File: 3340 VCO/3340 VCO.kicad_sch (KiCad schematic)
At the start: 99 parts, among them J1 AudioJack2_SwitchT, J2 AudioJack2_SwitchT, J3 AudioJack2_SwitchT, J4 AudioJack2_SwitchT, J5 AudioJack2_SwitchT, J6 Conn_02x05_Odd_Even, J7 AudioJack2_SwitchT, J8 AudioJack2_SwitchT, J9 AudioJack2_SwitchT, SW1 SW_SPDT, U1 TL072, U2 TL072, U3 TL072, U4 AS3340

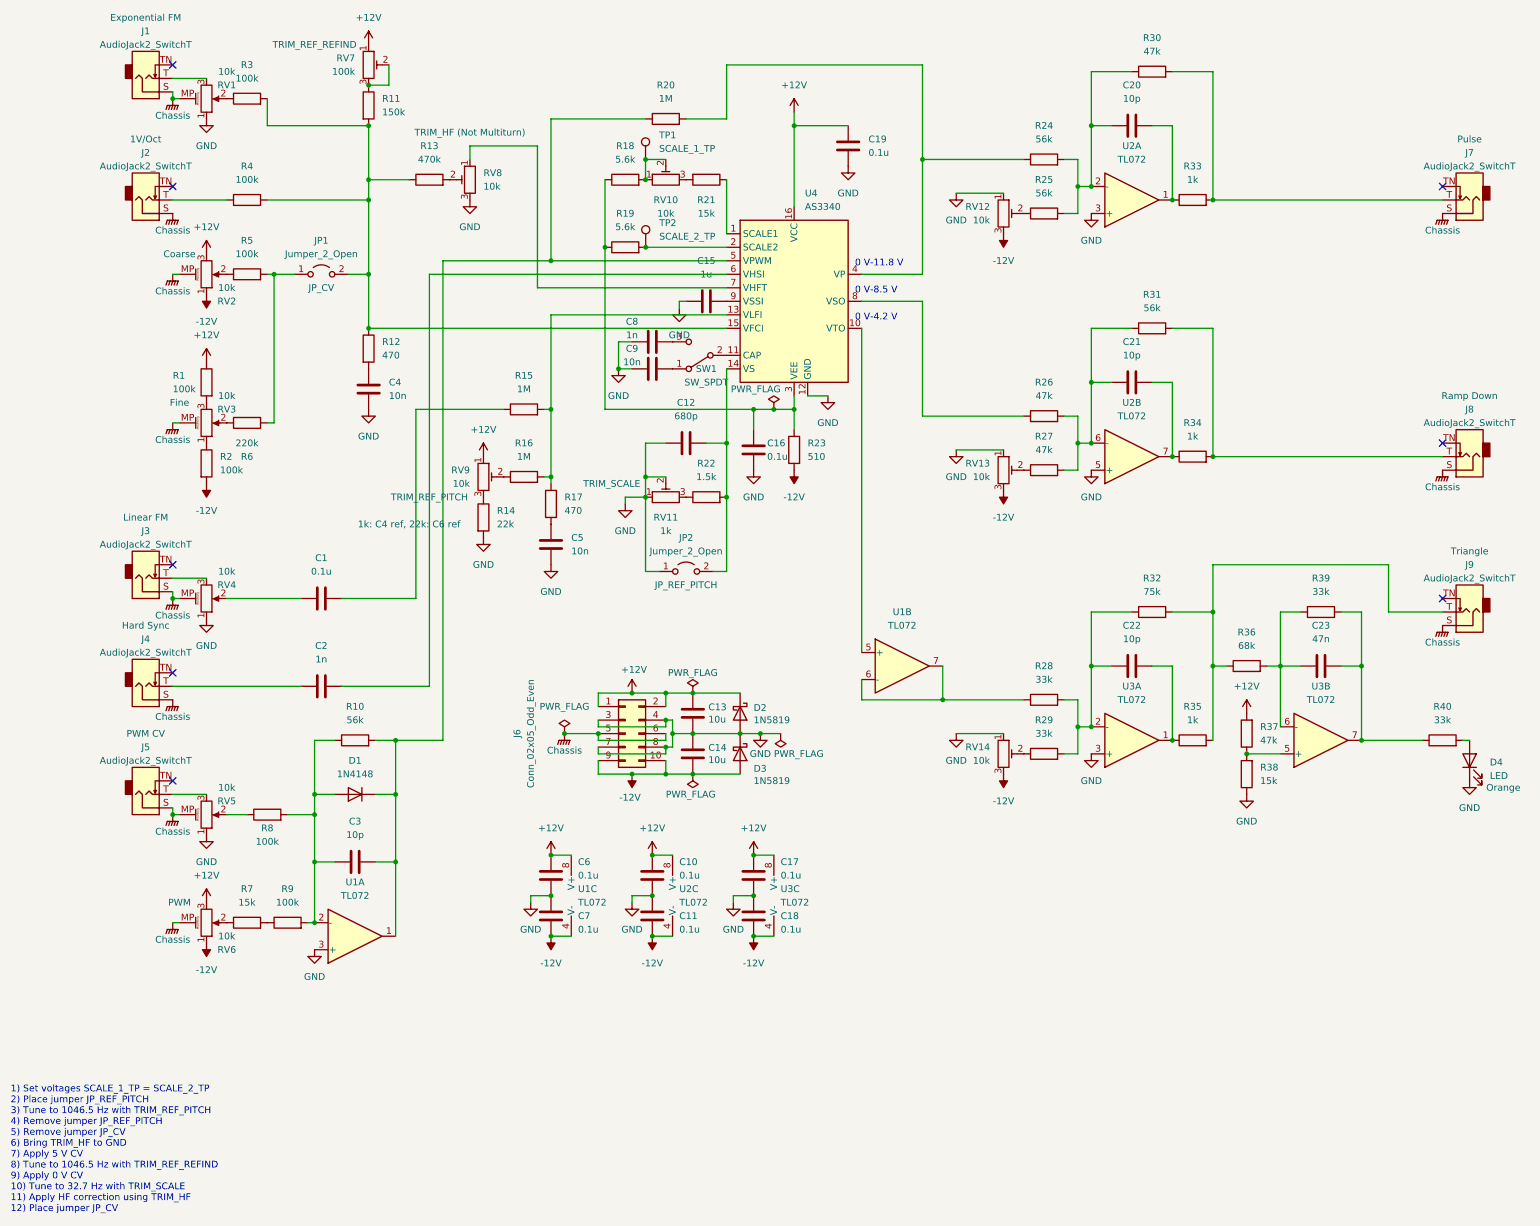
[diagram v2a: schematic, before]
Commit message: Create separate front end VCO board
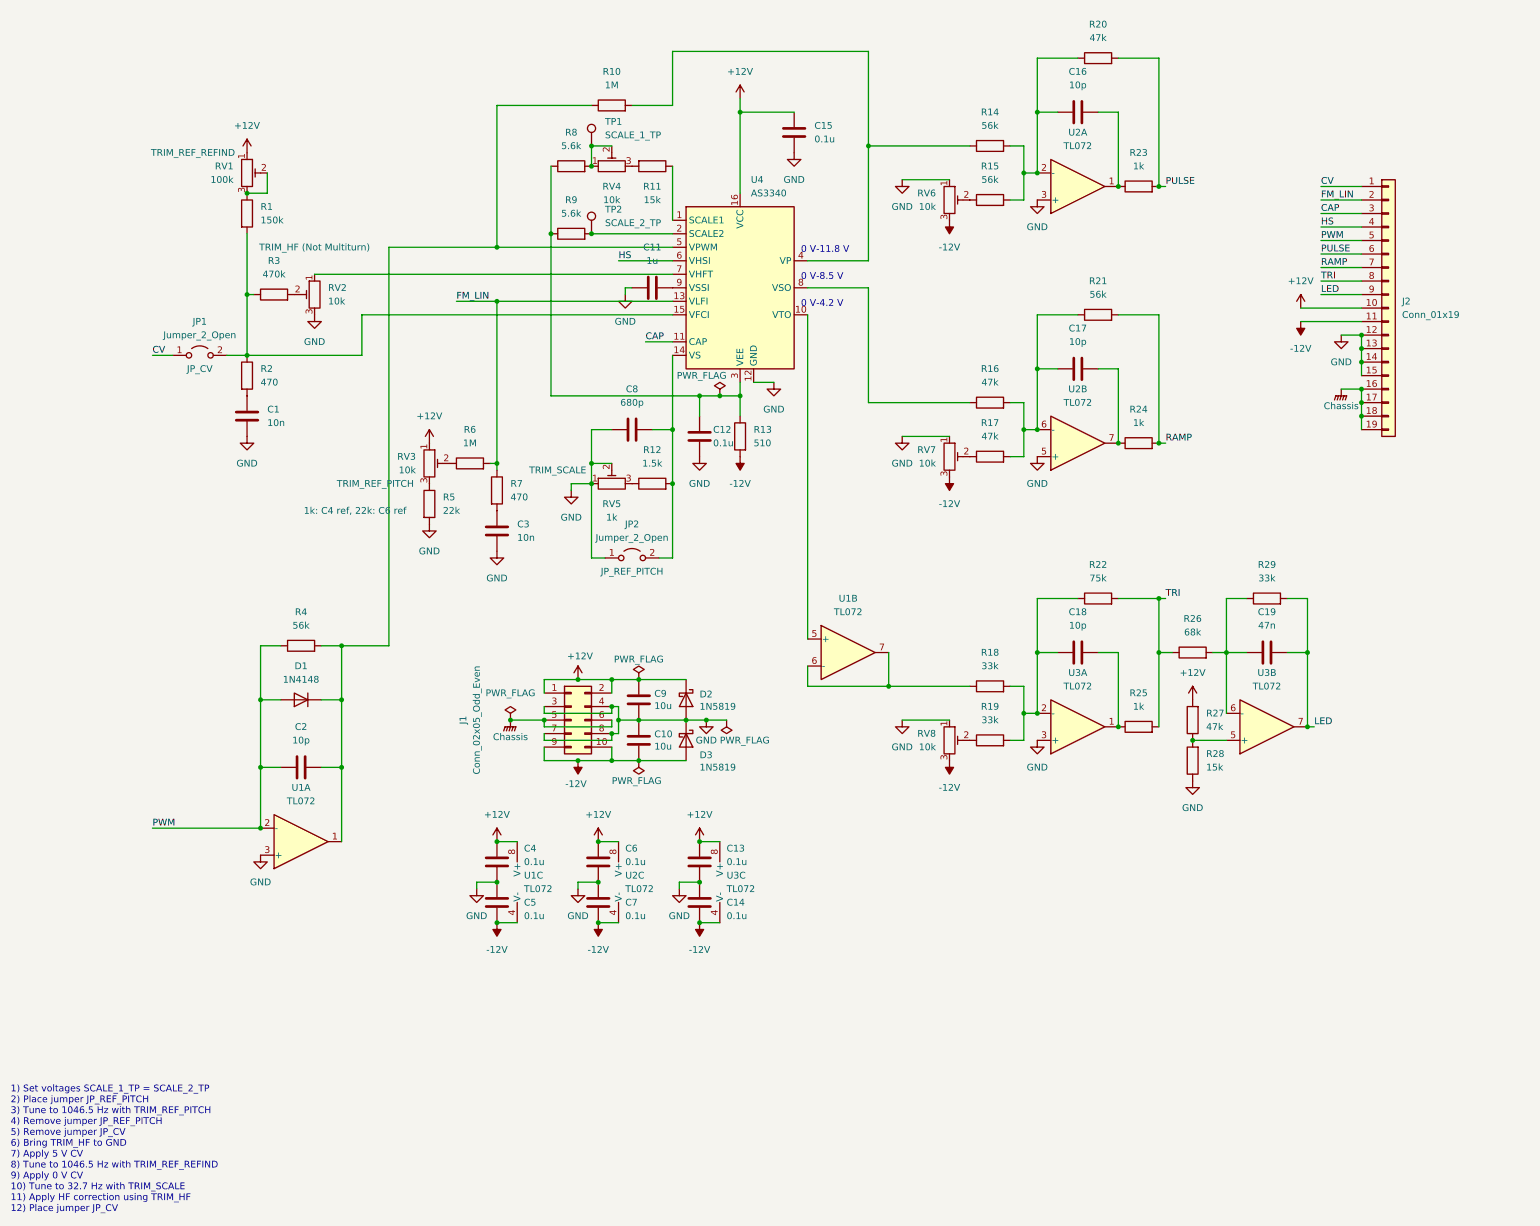
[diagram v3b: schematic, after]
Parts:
- removed C1: 0.1u, 0_Capacitor_THT:C_Disc_D5.5mm_W2.5mm_P2.50mm, symbol Device:C
- removed C2, C8: 1n, 0_Capacitor_THT:C_Disc_D5.5mm_W2.5mm_P2.50mm, symbol Device:C
- removed C9: 10n, 0_Capacitor_THT:C_Disc_D5.5mm_W2.5mm_P2.50mm, symbol Device:C
- removed D4: LED, LED_THT:LED_D5.0mm, symbol Device:LED
- removed J1, J2, J3, J4, J5, J7, J8, J9: AudioJack2_SwitchT, Connector_Audio:Jack_3.5mm_QingPu_WQP-PJ398SM_Vertical_CircularHoles, symbol Connector:AudioJack2_SwitchT
- removed R1, R2, R4, R5, R8, R9: 100k, Resistor_THT:R_Axial_DIN0207_L6.3mm_D2.5mm_P7.62mm_Horizontal, symbol Device:R
- removed R13: 470k, Resistor_THT:R_Axial_DIN0207_L6.3mm_D2.5mm_P7.62mm_Horizontal, symbol Device:R
- removed R15: 1M, Resistor_THT:R_Axial_DIN0207_L6.3mm_D2.5mm_P7.62mm_Horizontal, symbol Device:R
- removed R40: 33k, Resistor_THT:R_Axial_DIN0207_L6.3mm_D2.5mm_P7.62mm_Horizontal, symbol Device:R
- removed R6: 220k, Resistor_THT:R_Axial_DIN0207_L6.3mm_D2.5mm_P7.62mm_Horizontal, symbol Device:R
- removed R7: 15k, Resistor_THT:R_Axial_DIN0207_L6.3mm_D2.5mm_P7.62mm_Horizontal, symbol Device:R
- removed RV1, RV2, RV3, RV4, RV5, RV6: 10k, 0_Potentiometer_THT:Potentiometer_Alpha_RD901F-40-00D_Single_Vertical_MP, symbol Device:R_Potentiometer_MountingPin
- removed RV8: 10k, Potentiometer_THT:Potentiometer_Runtron_RM-065_Vertical, symbol Device:R_Potentiometer_Trim
- removed SW1: SW_SPDT, 0_Switch_THT:MTS-102_MTS-103_MTS-112_MTS-113_MTS-123, symbol Switch:SW_SPDT
- added J2: Conn_01x19, Connector_PinHeader_2.54mm:PinHeader_1x19_P2.54mm_Vertical, symbol Connector_Generic:Conn_01x19
- added RV2: 10k, Potentiometer_THT:Potentiometer_Runtron_RM-065_Vertical, symbol Device:R_Potentiometer_Trim
- R3: value 100k -> 470k
- renumbered C4 to C1, C14 to C10, C15 to C11, C16 to C12, C17 to C13, C18 to C14, C19 to C15, C20 to C16, C21 to C17, C22 to C18, C23 to C19, C3 to C2, C5 to C3, C6 to C4, C7 to C5, C10 to C6, C11 to C7, C12 to C8, C13 to C9, J6 to J1, R11 to R1, R20 to R10, R21 to R11, R22 to R12, R23 to R13, R24 to R14, R25 to R15, R26 to R16, R27 to R17, R28 to R18, R29 to R19, R12 to R2, R30 to R20, R31 to R21, R32 to R22, R33 to R23, R34 to R24, R35 to R25, R36 to R26, R37 to R27, R38 to R28, R39 to R29, R10 to R4, R14 to R5, R16 to R6, R17 to R7, R18 to R8, R19 to R9, RV7 to RV1, RV9 to RV3, RV10 to RV4, RV11 to RV5, RV12 to RV6, RV13 to RV7, RV14 to RV8
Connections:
- net +12V: now also J2.10 (Pin_10)
- net -12V: now also J2.11 (Pin_11)
- net Chassis: now also J2.16 (Pin_16), J2.17 (Pin_17), J2.18 (Pin_18), J2.19 (Pin_19)
- net GND: now also J2.12 (Pin_12), J2.13 (Pin_13), J2.14 (Pin_14), J2.15 (Pin_15), RV2.3
- net LED: now reaches C19.2, R29.2, U3.7
- net LED: now also J2.9 (Pin_9)
- net TRI: now reaches R22.2, R25.2, R26.1
- net TRI: now also J2.8 (Pin_8)
- net PWM: now reaches C2.1, D1.2 (A), R4.1, U1.2 (-)
- net PWM: now also J2.5 (Pin_5)
- net PULSE: now reaches R20.2, R23.2
- net PULSE: now also J2.6 (Pin_6)
- net at JP1.2 (B), R1.2, R2.1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: now also R3.1; no longer R3.2
- net CV: now reaches JP1.1 (A)
- net CV: now also J2.1 (Pin_1)
- net at U4.7 (VHFT): now also RV2.1
- net FM_LIN: now reaches R6.2, R7.1, U4.13 (VLFI)
- net FM_LIN: now also J2.2 (Pin_2)
- net HS: now reaches U4.6 (VHSI)
- net HS: now also J2.4 (Pin_4)
- net RAMP: now reaches R21.2, R24.2
- net RAMP: now also J2.7 (Pin_7)
- net CAP: now reaches U4.11 (CAP)
- net CAP: now also J2.3 (Pin_3)
- new net: R3.2, RV2.2
- no-connect marks 8 -> 0
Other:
- moved on the sheet: C1, C10, C11, C12, C13, C14, C15, C16, C17, C18, C19, C2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

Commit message: Add -5V regulator
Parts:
- removed R13: 510, Resistor_THT:R_Axial_DIN0207_L6.3mm_D2.5mm_P7.62mm_Horizontal, symbol Device:R
- added C15: 0.33u, 0_Capacitor_THT:C_Disc_D5.5mm_W2.5mm_P2.50mm, symbol Device:C
- added C17: 1u, 0_Capacitor_THT:C_Disc_D5.5mm_W4.0mm_P2.50mm, symbol Device:C
- added U5: MC7905, Package_TO_SOT_THT:TO-220-3_Vertical, symbol Regulator_Linear:MC7905
- renumbered C8 to C10, C9 to C11, C10 to C12, C11 to C13, C12 to C14, C15 to C16, C16 to C18, C17 to C19, C18 to C20, C19 to C21, C4 to C3, C5 to C4, C3 to C5, C13 to C8, C14 to C9, R14 to R13, R15 to R14, R16 to R15, R17 to R16, R18 to R17, R19 to R18, R20 to R19, R21 to R20, R22 to R21, R23 to R22, R24 to R23, R25 to R24, R26 to R25, R27 to R26, R28 to R27, R29 to R28
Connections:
- net -12V: now also C15.2, U5.2 (VI)
- net GND: now also C15.1, C17.1, U5.1 (GND)
- net -5V: now reaches C14.2, R8.1, R9.1, U4.3 (VEE)
- net -5V: now also C17.2, U5.3 (VO)
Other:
- moved on the sheet: C14, C3, C4, C6, C7, C8, C9, U1C, U2C, U3C

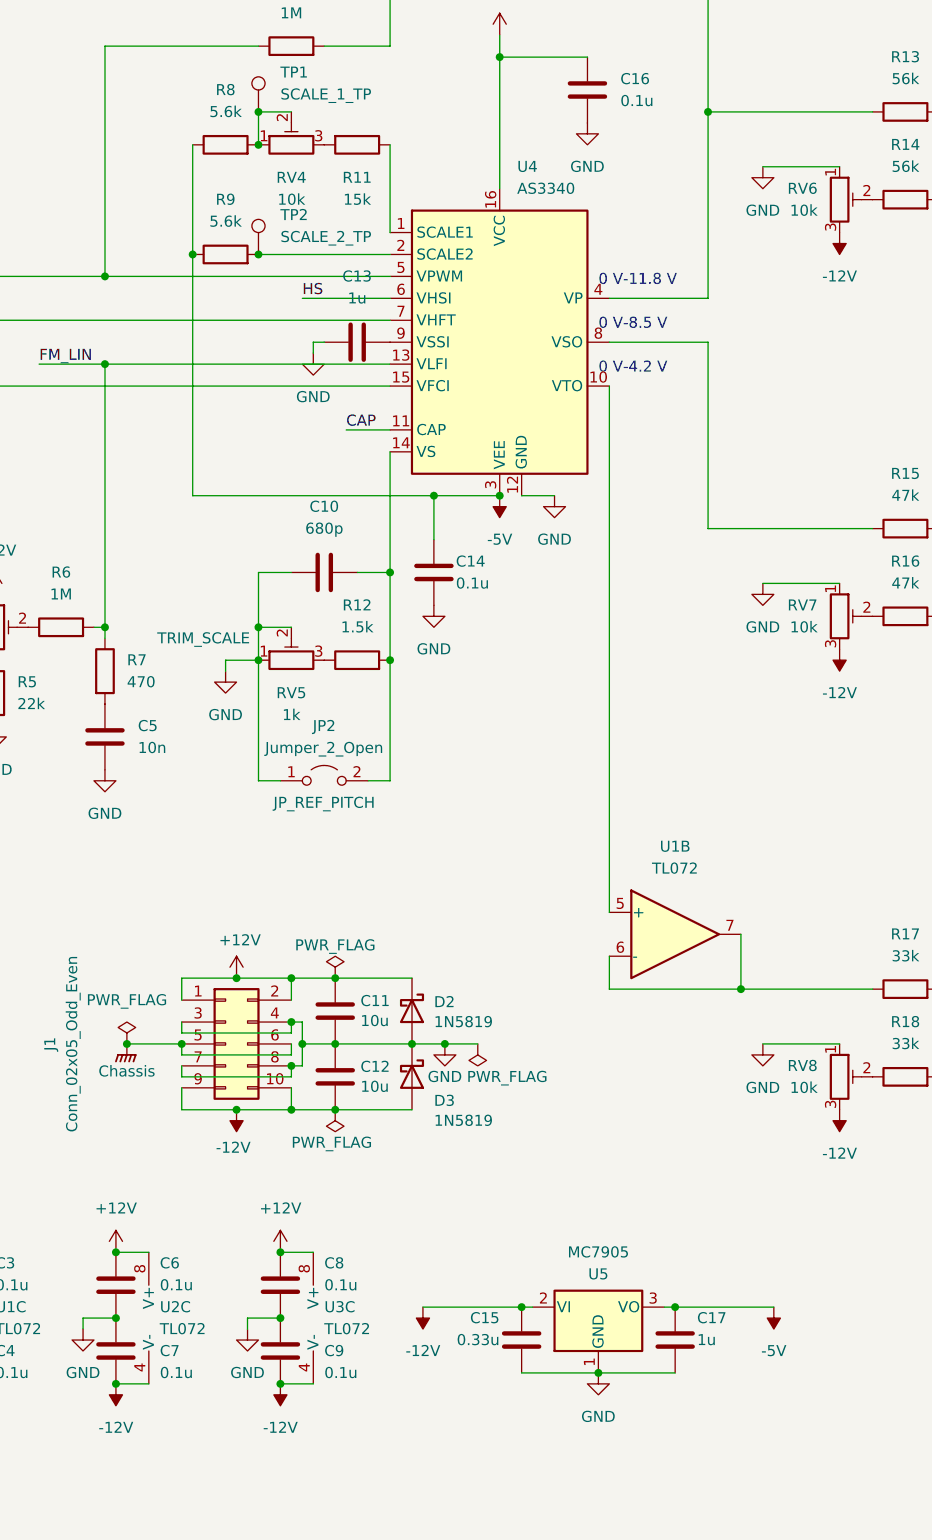
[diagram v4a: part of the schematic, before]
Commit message: Add precision R and C notes, update -5V regulator
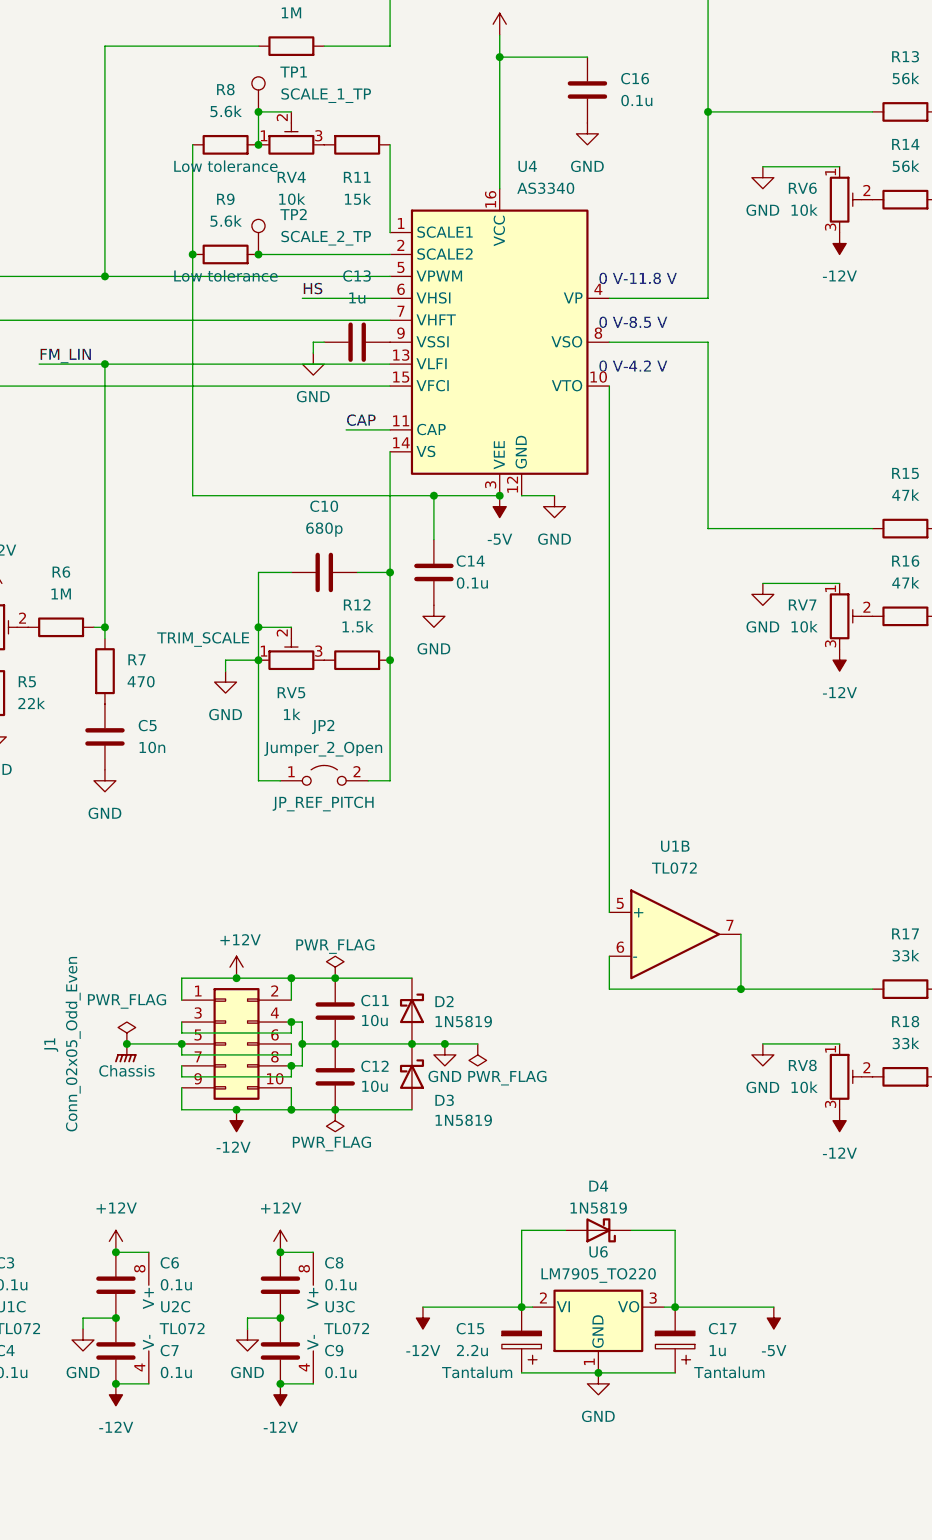
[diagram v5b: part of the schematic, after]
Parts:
- removed C15: 0.33u, 0_Capacitor_THT:C_Disc_D5.5mm_W2.5mm_P2.50mm, symbol Device:C
- removed C17: 1u, 0_Capacitor_THT:C_Disc_D5.5mm_W4.0mm_P2.50mm, symbol Device:C
- removed U5: MC7905, Package_TO_SOT_THT:TO-220-3_Vertical, symbol Regulator_Linear:MC7905
- added C15: 2.2u, symbol Device:C_Polarized
- added C17: 1u, symbol Device:C_Polarized
- added D4: 1N5819, Diode_THT:D_DO-41_SOD81_P10.16mm_Horizontal, symbol Diode:1N5819
- added U6: LM7905_TO220, Package_TO_SOT_THT:TO-220-3_Vertical, symbol Regulator_Linear:LM7905_TO220
- R8, R9: Notes (none) -> Low tolerance
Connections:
- net -12V: now also C15.2, D4.2 (A), U6.2 (VI)
- net -5V: now also C17.2, D4.1 (K), U6.3 (VO)
- net GND: now also C15.1, C17.1, U6.1 (GND)

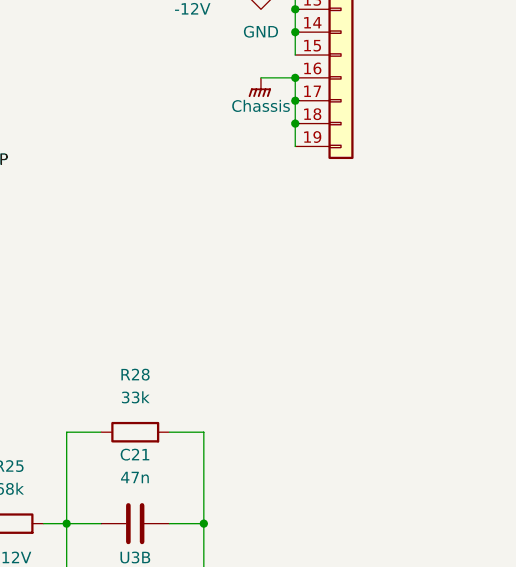
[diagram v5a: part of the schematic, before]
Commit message: Update VCO capacitor selection
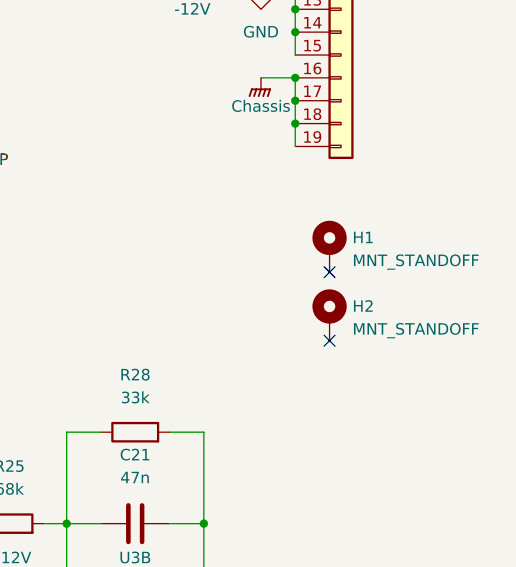
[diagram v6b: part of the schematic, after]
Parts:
- added H1, H2: MNT_STANDOFF, 0_MountingHole:MountingHole_Pitch7.5mm_Drill3.4mm, symbol Mechanical:MountingHole_Pad
- C15: footprint (none) -> Capacitor_THT:CP_Radial_Tantal_D5.5mm_P2.50mm
- C17: footprint (none) -> Capacitor_THT:CP_Radial_Tantal_D5.0mm_P2.50mm
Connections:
- no-connect marks 0 -> 2
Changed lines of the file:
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@@
   (junction (at 215.9 45.72) (diameter 0) (color 0 0 0 0)
   )
+  (no_connect (at 257.81 105.41))
+  (no_connect (at 257.81 113.03))
   (wire (pts (xy 165.1 139.7) (xy 180.34 139.7))
     (stroke (width 0) (type default))
@@
       (effects (font (size 1.27 1.27)) (justify right))
     )
-    (property "Footprint" "" (at 156.5148 176.53 0)
+    (property "Footprint" "Capacitor_THT:CP_Radial_Tantal_D5.0mm_P2.50mm" (at 156.5148 176.53 0)
       (effects (font (size 1.27 1.27)) hide)
     )
@@
     )
   )
+  (symbol (lib_id "Mechanical:MountingHole_Pad") (at 257.81 110.49 0) (unit 1)
+    (in_bom yes) (on_board yes) (dnp no) (fields_autoplaced)
+    (property "Reference" "H2" (at 260.35 109.22 0)
+      (effects (font (size 1.27 1.27)) (justify left))
+    )
+    (property "Value" "MNT_STANDOFF" (at 260.35 111.76 0)
+      (effects (font (size 1.27 1.27)) (justify left))
+    )
+    (property "Footprint" "0_MountingHole:MountingHole_Pitch7.5mm_Drill3.4mm" (at 257.81 110.49 0)
+      (effects (font (size 1.27 1.27)) hide)
+    )
+    (property "Datasheet" "~" (at 257.81 110.49 0)
+      (effects (font (size 1.27 1.27)) hide)
+    )
+    (pin "1")
+    (instances
+      (project "3340 VCO"
+        (path "/9405806f-66a1-4b59-a7df-b7e75584f762"
+          (reference "H2") (unit 1)
+        )
+      )
+      (project "Front End"
+        (path "/a1c7a80e-571d-4d37-b0fe-6f3972cbd9bc"
+          (reference "H2") (unit 1)
+        )
+      )
+    )
+  )
   (symbol (lib_id "power:GND") (at 69.85 179.07 0) (unit 1)
     (in_bom yes) (on_board yes) (dnp no) (fields_autoplaced)
@@
       (effects (font (size 1.27 1.27)) (justify right))
     )
-    (property "Footprint" "" (at 138.7348 176.53 0)
+    (property "Footprint" "Capacitor_THT:CP_Radial_Tantal_D5.5mm_P2.50mm" (at 138.7348 176.53 0)
       (effects (font (size 1.27 1.27)) hide)
     )
@@
         )
       )
+    )
+  )
+  (symbol (lib_id "Mechanical:MountingHole_Pad") (at 257.81 102.87 0) (unit 1)
+    (in_bom yes) (on_board yes) (dnp no) (fields_autoplaced)
+    (property "Reference" "H1" (at 260.35 101.6 0)
+      (effects (font (size 1.27 1.27)) (justify left))
+    )
+    (property "Value" "MNT_STANDOFF" (at 260.35 104.14 0)
+      (effects (font (size 1.27 1.27)) (justify left))
+    )
+    (property "Footprint" "0_MountingHole:MountingHole_Pitch7.5mm_Drill3.4mm" (at 257.81 102.87 0)
+      (effects (font (size 1.27 1.27)) hide)
+    )
+    (property "Datasheet" "~" (at 257.81 102.87 0)
+      (effects (font (size 1.27 1.27)) hide)
+    )
+    (pin "1")
+    (instances
+      (project "3340 VCO"
+        (path "/9405806f-66a1-4b59-a7df-b7e75584f762"
+          (reference "H1") (unit 1)
+        )
+      )
+      (project "Front End"
+        (path "/a1c7a80e-571d-4d37-b0fe-6f3972cbd9bc"
+          (reference "H1") (unit 1)
+        )
+      )
